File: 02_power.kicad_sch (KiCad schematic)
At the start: 22 parts, among them J5 2171790001, J6 Conn_01x02_Socket, Q2 DMG2305UX-7, U2 BQ24090DGQ

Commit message: Worked on Design, eliminating errors
Signed-off-by: Anna-Lena Marx <anna-lena.marx@web.de>
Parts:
- J6: footprint Connector_JST:JST_EH_S2B-EH_1x02_P2.50mm_Horizontal -> Connector_JST:JST_PH_S2B-PH-K_1x02_P2.00mm_Horizontal
- renumbered TP13 to TP13_USB_VBUS1, TP14 to TP14_USB_LIPO1, TP15 to TP15_VSYS1, TP16 to TP16_GND1
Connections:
- net GND: now also J6.2 (Pin_2); no longer J6.1 (Pin_1)
- net V_USB_LIPO: now also J6.1 (Pin_1); no longer J6.2 (Pin_2)
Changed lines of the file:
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@@
 	)
 	(junction
+		(at 140.97 88.9)
+		(diameter 0)
+		(color 0 0 0 0)
+	)
+	(junction
 		(at 24.13 99.06)
 		(diameter 0)
@@
 	)
 	(junction
-		(at 140.97 88.9)
-		(diameter 0)
-		(color 0 0 0 0)
-	)
-	(junction
 		(at 53.34 55.88)
 		(diameter 0)
@@
 	(wire
 		(pts
-			(xy 140.97 88.9) (xy 151.13 88.9)
-		)
-		(stroke
-			(width 0)
-			(type default)
-		)
-	)
-	(wire
-		(pts
 			(xy 83.82 85.09) (xy 83.82 104.14)
 		)
@@
 	(wire
 		(pts
+			(xy 140.97 88.9) (xy 151.13 88.9)
+		)
+		(stroke
+			(width 0)
+			(type default)
+		)
+	)
+	(wire
+		(pts
 			(xy 105.41 72.39) (xy 92.71 72.39)
 		)
@@
 		(dnp no)
 		(fields_autoplaced yes)
-		(property "Reference" "TP14"
+		(property "Reference" "TP14_USB_LIPO1"
 			(at 73.66 170.1799 90)
 			(effects
@@
 			(project "ZEReader-Pico"
 				(path "/ec954637-2a8b-4662-b4a1-f88107f11cb0/a18230d5-251f-4044-a9cd-045093d87cd6"
-					(reference "TP14")
+					(reference "TP14_USB_LIPO1")
 					(unit 1)
 				)
@@
 	)
 	(symbol
+		(lib_id "Connector:Conn_01x02_Socket")
+		(at 156.21 86.36 0)
+		(unit 1)
+		(exclude_from_sim no)
+		(in_bom yes)
+		(on_board yes)
+		(dnp no)
+		(property "Reference" "J6"
+			(at 157.48 86.3599 0)
+			(effects
+				(font
+					(size 1.27 1.27)
+				)
+				(justify left)
+			)
+		)
+		(property "Value" "Conn_01x02_Socket"
+			(at 157.48 88.8999 0)
+			(effects
+				(font
+					(size 1.27 1.27)
+				)
+				(justify left)
+			)
+		)
+		(property "Footprint" "Connector_JST:JST_PH_S2B-PH-K_1x02_P2.00mm_Horizontal"
+			(at 156.21 86.36 0)
+			(effects
+				(font
+					(size 1.27 1.27)
+				)
+				(hide yes)
+			)
+		)
+		(property "Datasheet" "~"
+			(at 156.21 86.36 0)
+			(effects
+				(font
+					(size 1.27 1.27)
+				)
+				(hide yes)
+			)
+		)
+		(property "Description" "Generic connector, single row, 01x02, script generated"
+			(at 156.21 86.36 0)
+			(effects
+				(font
+					(size 1.27 1.27)
+				)
+				(hide yes)
+			)
+		)
+		(pin "2"
+		)
+		(pin "1"
+		)
+		(instances
+			(project ""
+				(path "/ec954637-2a8b-4662-b4a1-f88107f11cb0/a18230d5-251f-4044-a9cd-045093d87cd6"
+					(reference "J6")
+					(unit 1)
+				)
+			)
+		)
+	)
+	(symbol
 		(lib_id "Battery_Management:BQ24090DGQ")
 		(at 118.11 69.85 0)
@@
 	)
 	(symbol
-		(lib_id "Connector:Conn_01x02_Socket")
-		(at 156.21 88.9 0)
-		(mirror x)
-		(unit 1)
-		(exclude_from_sim no)
-		(in_bom yes)
-		(on_board yes)
-		(dnp no)
-		(property "Reference" "J6"
-			(at 157.48 88.9001 0)
-			(effects
-				(font
-					(size 1.27 1.27)
-				)
-				(justify left)
-			)
-		)
-		(property "Value" "Conn_01x02_Socket"
-			(at 157.48 86.3601 0)
-			(effects
-				(font
-					(size 1.27 1.27)
-				)
-				(justify left)
-			)
-		)
-		(property "Footprint" "Connector_JST:JST_EH_S2B-EH_1x02_P2.50mm_Horizontal"
-			(at 156.21 88.9 0)
-			(effects
-				(font
-					(size 1.27 1.27)
-				)
-				(hide yes)
-			)
-		)
-		(property "Datasheet" "~"
-			(at 156.21 88.9 0)
-			(effects
-				(font
-					(size 1.27 1.27)
-				)
-				(hide yes)
-			)
-		)
-		(property "Description" "Generic connector, single row, 01x02, script generated"
-			(at 156.21 88.9 0)
-			(effects
-				(font
-					(size 1.27 1.27)
-				)
-				(hide yes)
-			)
-		)
-		(pin "2"
-		)
-		(pin "1"
-		)
-		(instances
-			(project ""
-				(path "/ec954637-2a8b-4662-b4a1-f88107f11cb0/a18230d5-251f-4044-a9cd-045093d87cd6"
-					(reference "J6")
-					(unit 1)
-				)
-			)
-		)
-	)
-	(symbol
 		(lib_id "DMG2305UX-7:DMG2305UX-7")
 		(at 207.01 64.77 90)
@@
 		(dnp no)
 		(fields_autoplaced yes)
-		(property "Reference" "TP13"
+		(property "Reference" "TP13_USB_VBUS1"
 			(at 73.66 163.8299 90)
 			(effects
@@
 			(project ""
 				(path "/ec954637-2a8b-4662-b4a1-f88107f11cb0/a18230d5-251f-4044-a9cd-045093d87cd6"
-					(reference "TP13")
+					(reference "TP13_USB_VBUS1")
 					(unit 1)
 				)
@@
 		(dnp no)
 		(fields_autoplaced yes)
-		(property "Reference" "TP16"
+		(property "Reference" "TP16_GND1"
 			(at 73.66 182.8799 90)
 			(effects
@@
 			(project "ZEReader-Pico"
 				(path "/ec954637-2a8b-4662-b4a1-f88107f11cb0/a18230d5-251f-4044-a9cd-045093d87cd6"
-					(reference "TP16")
+					(reference "TP16_GND1")
 					(unit 1)
 				)
@@
 		(dnp no)
 		(fields_autoplaced yes)
-		(property "Reference" "TP15"
+		(property "Reference" "TP15_VSYS1"
 			(at 73.66 176.5299 90)
 			(effects
@@
 			(project "ZEReader-Pico"
 				(path "/ec954637-2a8b-4662-b4a1-f88107f11cb0/a18230d5-251f-4044-a9cd-045093d87cd6"
-					(reference "TP15")
+					(reference "TP15_VSYS1")
 					(unit 1)
 				)

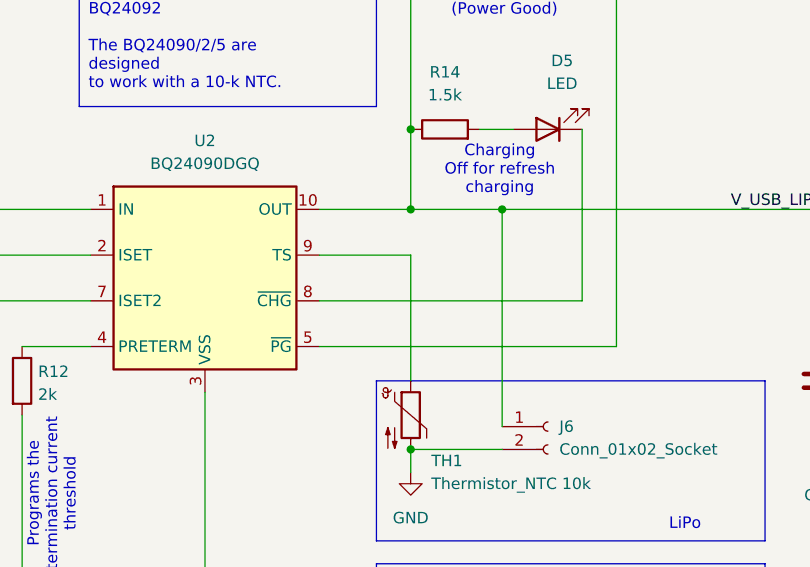
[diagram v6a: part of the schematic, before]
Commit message: Rerouted whole PCB
Signed-off-by: Anna-Lena Marx <anna-lena.marx@web.de>
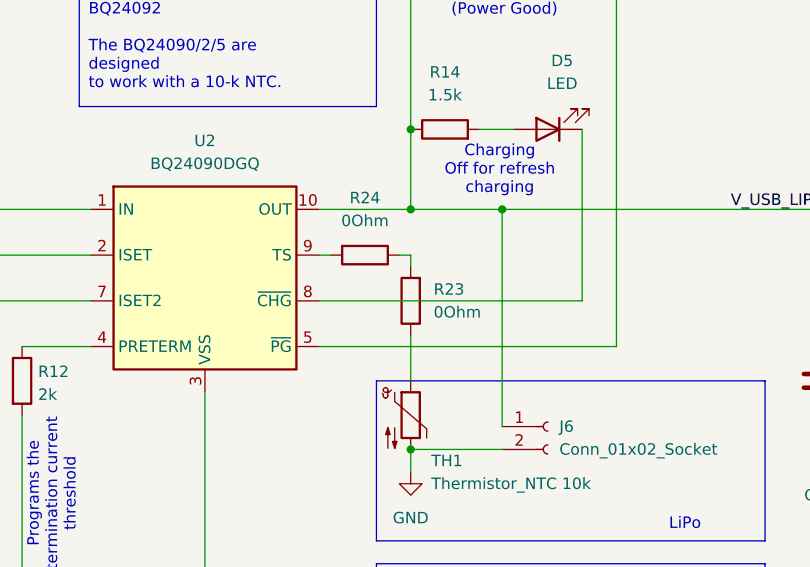
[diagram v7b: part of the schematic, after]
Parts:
- added R23, R24: 0Ohm, Resistor_SMD:R_1206_3216Metric_Pad1.30x1.75mm_HandSolder, symbol Device:R
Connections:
- net at U2.9 (TS): now also R24.2; no longer TH1.1
- new net: R23.2, R24.1
- new net: R23.1, TH1.1
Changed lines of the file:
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@@
 	(wire
 		(pts
+			(xy 140.97 76.2) (xy 140.97 81.28)
+		)
+		(stroke
+			(width 0)
+			(type default)
+		)
+	)
+	(wire
+		(pts
 			(xy 34.29 55.88) (xy 31.75 55.88)
 		)
@@
 	(wire
 		(pts
-			(xy 140.97 67.31) (xy 130.81 67.31)
-		)
-		(stroke
-			(width 0)
-			(type default)
-		)
-	)
-	(wire
-		(pts
 			(xy 151.13 62.23) (xy 151.13 86.36)
 		)
@@
 	(wire
 		(pts
-			(xy 140.97 81.28) (xy 140.97 67.31)
+			(xy 130.81 67.31) (xy 132.08 67.31)
+		)
+		(stroke
+			(width 0)
+			(type default)
+		)
+	)
+	(wire
+		(pts
+			(xy 139.7 67.31) (xy 140.97 67.31)
 		)
 		(stroke
@@
 	(wire
 		(pts
+			(xy 140.97 67.31) (xy 140.97 68.58)
+		)
+		(stroke
+			(width 0)
+			(type default)
+		)
+	)
+	(wire
+		(pts
 			(xy 54.61 104.14) (xy 71.12 104.14)
 		)
@@
 	)
 	(symbol
+		(lib_id "Device:R")
+		(at 135.89 67.31 270)
+		(unit 1)
+		(exclude_from_sim no)
+		(in_bom yes)
+		(on_board yes)
+		(dnp no)
+		(fields_autoplaced yes)
+		(property "Reference" "R24"
+			(at 135.89 60.96 90)
+			(effects
+				(font
+					(size 1.27 1.27)
+				)
+			)
+		)
+		(property "Value" "0Ohm"
+			(at 135.89 63.5 90)
+			(effects
+				(font
+					(size 1.27 1.27)
+				)
+			)
+		)
+		(property "Footprint" "Resistor_SMD:R_1206_3216Metric_Pad1.30x1.75mm_HandSolder"
+			(at 135.89 65.532 90)
+			(effects
+				(font
+					(size 1.27 1.27)
+				)
+				(hide yes)
+			)
+		)
+		(property "Datasheet" "~"
+			(at 135.89 67.31 0)
+			(effects
+				(font
+					(size 1.27 1.27)
+				)
+				(hide yes)
+			)
+		)
+		(property "Description" "Resistor"
+			(at 135.89 67.31 0)
+			(effects
+				(font
+					(size 1.27 1.27)
+				)
+				(hide yes)
+			)
+		)
+		(pin "1"
+		)
+		(pin "2"
+		)
+		(instances
+			(project "ZEReader-Pico"
+				(path "/ec954637-2a8b-4662-b4a1-f88107f11cb0/a18230d5-251f-4044-a9cd-045093d87cd6"
+					(reference "R24")
+					(unit 1)
+				)
+			)
+		)
+	)
+	(symbol
 		(lib_id "DMG2305UX-7:DMG2305UX-7")
 		(at 207.01 64.77 90)
@@
 					(unit 1)
 				)
+			)
+		)
+	)
+	(symbol
+		(lib_id "Device:R")
+		(at 140.97 72.39 180)
+		(unit 1)
+		(exclude_from_sim no)
+		(in_bom yes)
+		(on_board yes)
+		(dnp no)
+		(fields_autoplaced yes)
+		(property "Reference" "R23"
+			(at 143.51 71.1199 0)
+			(effects
+				(font
+					(size 1.27 1.27)
+				)
+				(justify right)
+			)
+		)
+		(property "Value" "0Ohm"
+			(at 143.51 73.6599 0)
+			(effects
+				(font
+					(size 1.27 1.27)
+				)
+				(justify right)
+			)
+		)
+		(property "Footprint" "Resistor_SMD:R_1206_3216Metric_Pad1.30x1.75mm_HandSolder"
+			(at 142.748 72.39 90)
+			(effects
+				(font
+					(size 1.27 1.27)
+				)
+				(hide yes)
+			)
+		)
+		(property "Datasheet" "~"
+			(at 140.97 72.39 0)
+			(effects
+				(font
+					(size 1.27 1.27)
+				)
+				(hide yes)
+			)
+		)
+		(property "Description" "Resistor"
+			(at 140.97 72.39 0)
+			(effects
+				(font
+					(size 1.27 1.27)
+				)
+				(hide yes)
+			)
+		)
+		(pin "1"
+		)
+		(pin "2"
+		)
+		(instances
+			(project ""
+				(path "/ec954637-2a8b-4662-b4a1-f88107f11cb0/a18230d5-251f-4044-a9cd-045093d87cd6"
+					(reference "R23")
+					(unit 1)
+				)

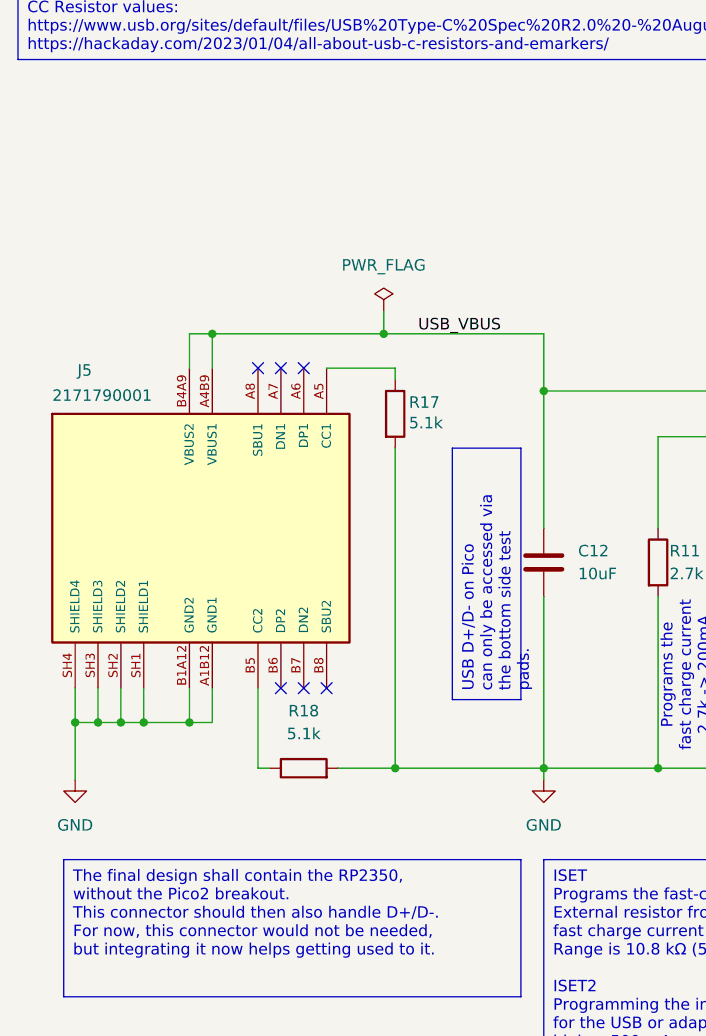
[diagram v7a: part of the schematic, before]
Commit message: Changed USB-C connector due to availability issues
Signed-off-by: Anna-Lena Marx <anna-lena.marx@web.de>
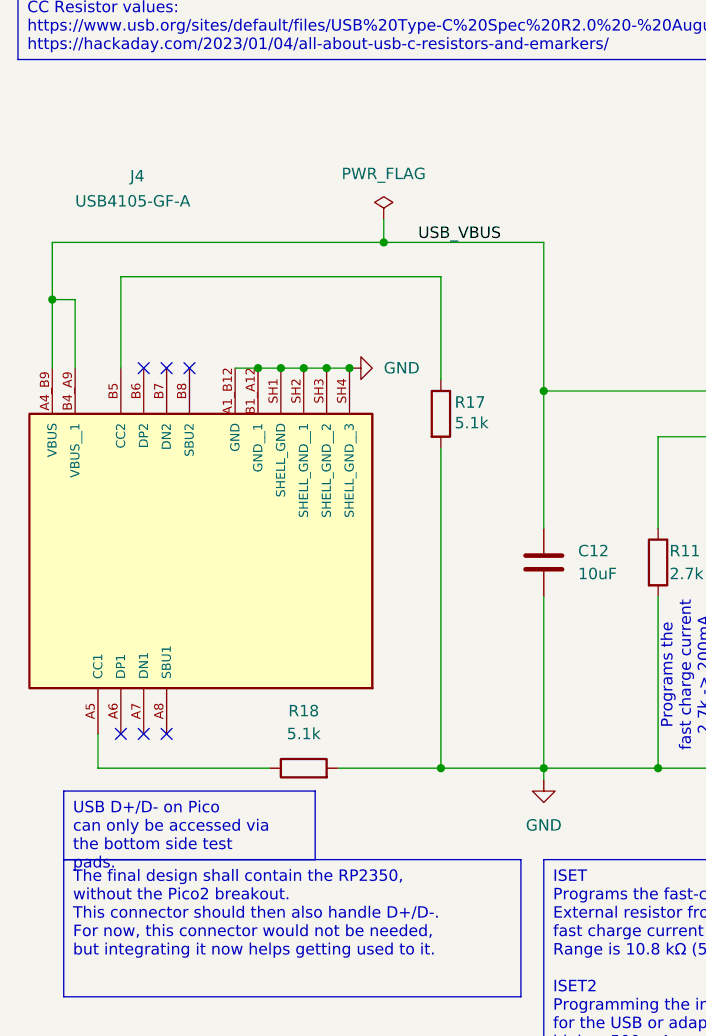
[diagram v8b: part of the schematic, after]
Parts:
- removed J5: 2171790001, prj-footprints:MOLEX_2171790001, symbol 2171790001:2171790001
- added J4: USB4105-GF-A, prj-footprints:GCT_USB4105-GF-A, symbol USB4105-GF-A:USB4105-GF-A
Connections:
- net GND: now also J4.A1_B12 (GND), J4.B1_A12 (GND__1), J4.SH1 (SHELL_GND), J4.SH2 (SHELL_GND__1), J4.SH3 (SHELL_GND__2), J4.SH4 (SHELL_GND__3)
- net USB_VBUS: now also J4.A4_B9 (VBUS), J4.B4_A9 (VBUS__1)
- net at R18.1: now also J4.A5 (CC1)
- net at R17.1: now also J4.B5 (CC2)
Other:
- moved on the sheet: R17
